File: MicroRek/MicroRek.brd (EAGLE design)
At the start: 40 x 30 mm, 41 parts, among them IC3 LSM9DS1TR

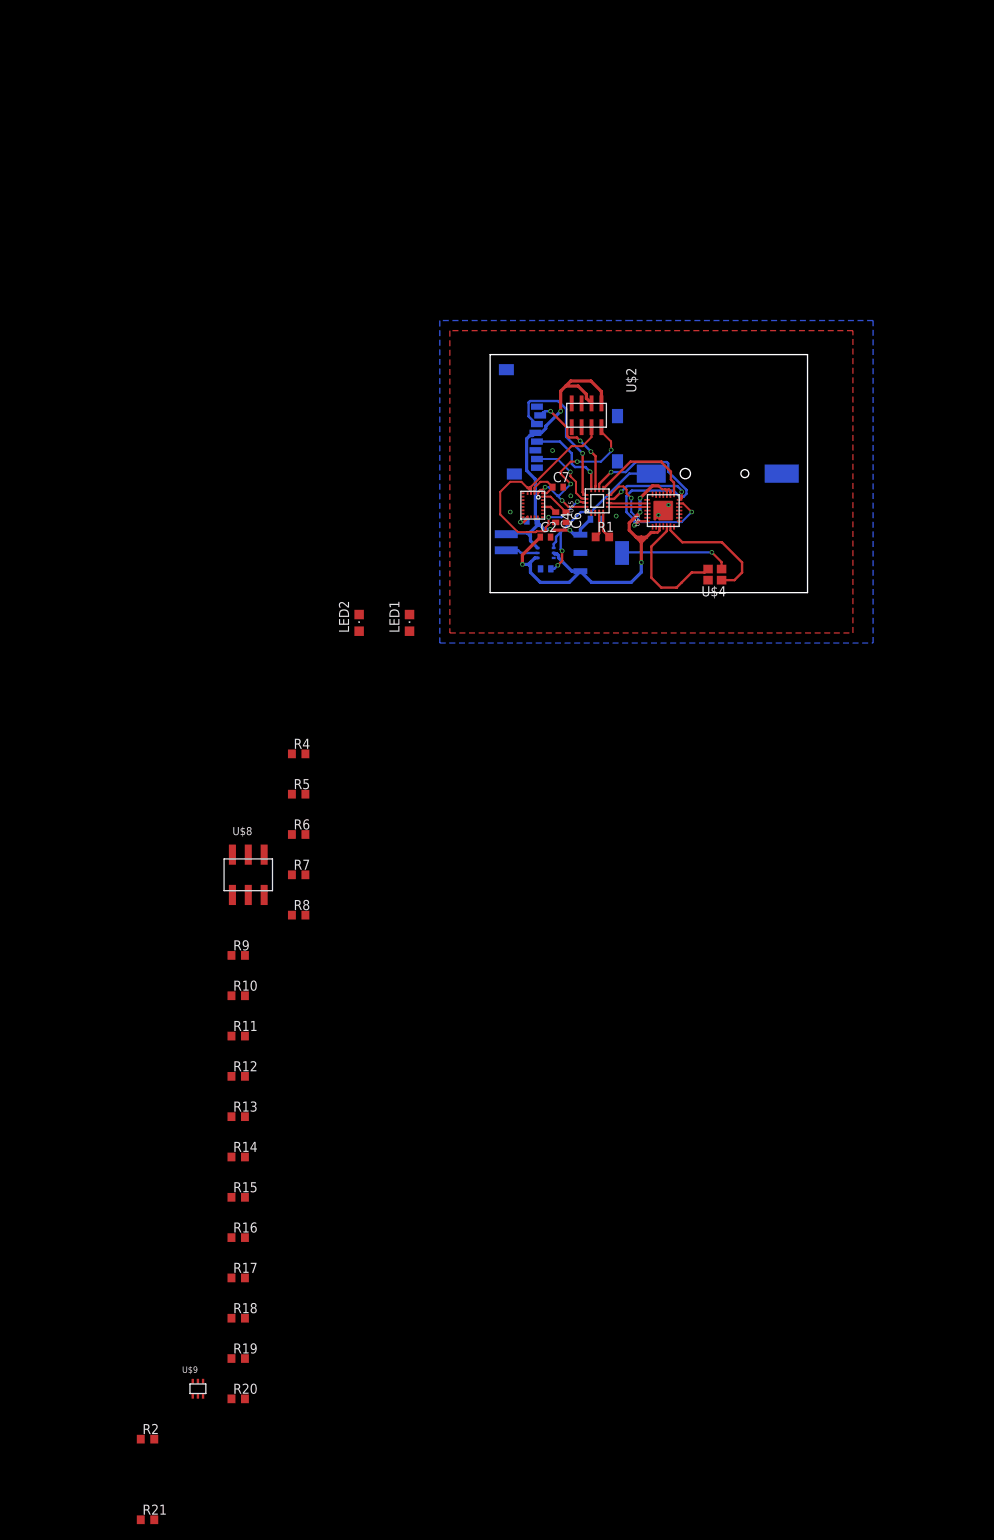
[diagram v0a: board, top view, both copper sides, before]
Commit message: fixed pullup resistors
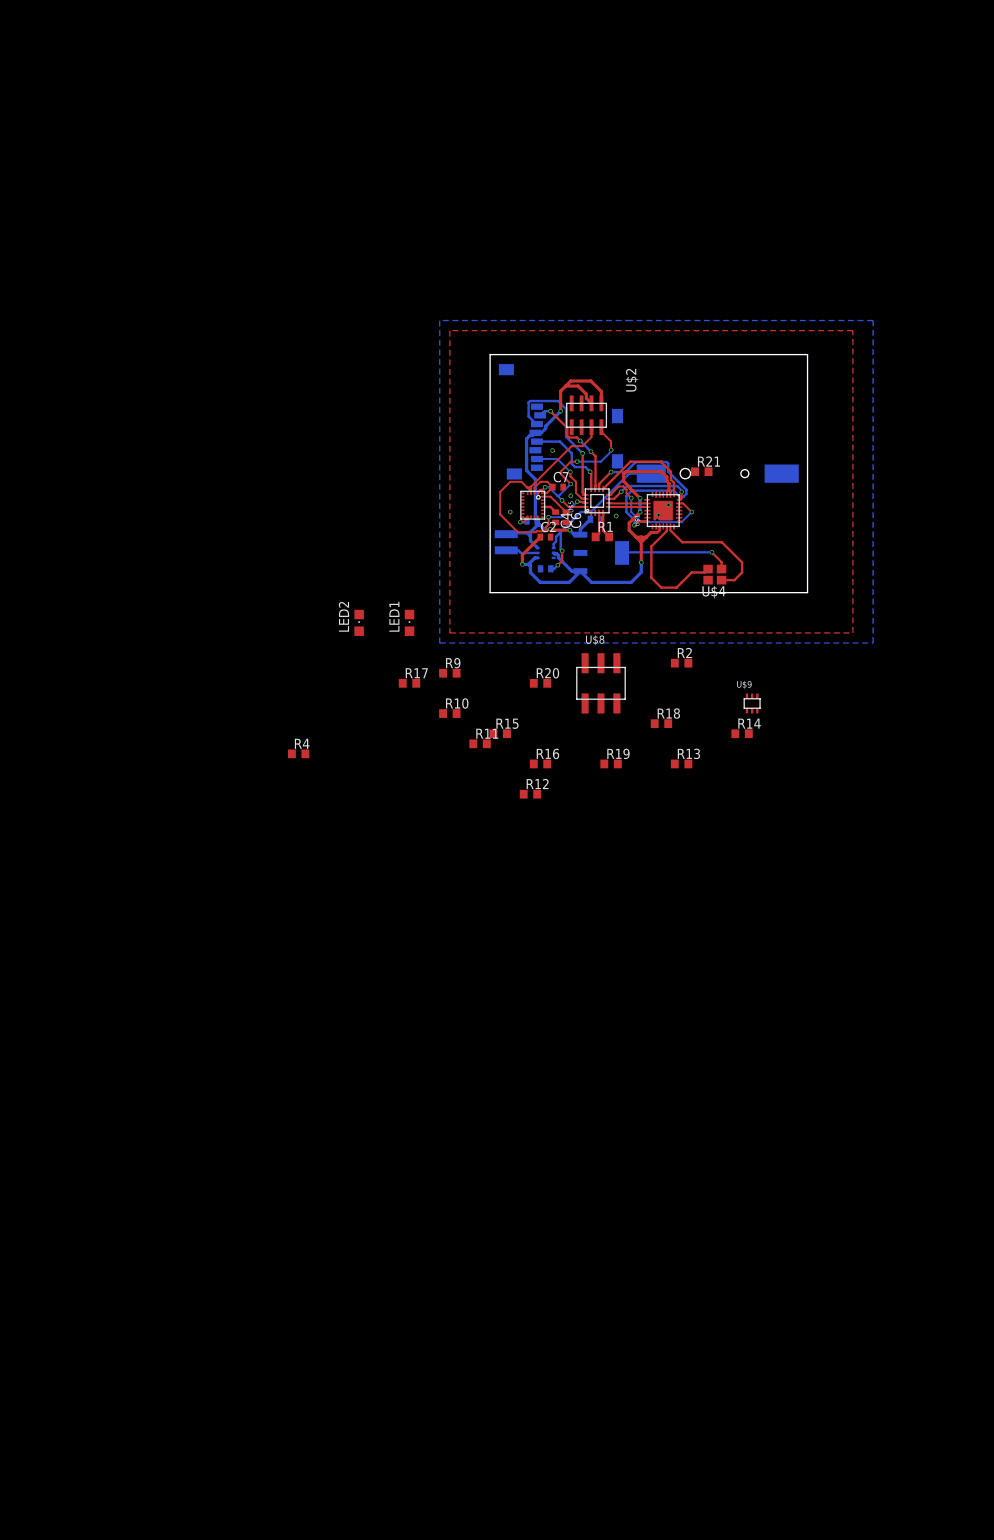
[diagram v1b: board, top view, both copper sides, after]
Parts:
- removed R5, R6, R7, R8: 10kΩ, resistor:R0603
- moved R21 149.4 mm to (26.7, 15.2)
- moved R2 118.7 mm to (24.1, -8.89)
- moved U$9 111.1 mm to (33.0, -14.0)
- moved R20 97.9 mm to (6.35, -11.4)
- moved R18 92.0 mm to (21.6, -16.5)
- moved R19 88.4 mm to (15.2, -21.6)
- moved R14 82.9 mm to (31.8, -17.8)
- moved R17 78.0 mm to (-10.2, -11.4)
- moved R13 71.4 mm to (24.1, -21.6)
- moved R16 70.8 mm to (6.35, -21.6)
- moved R15 67.1 mm to (1.27, -17.8)
- moved R12 51.2 mm to (5.08, -25.4)
- moved U$8 50.6 mm to (14.0, -11.4)
- moved R11 47.8 mm to (-1.27, -19.1)
- moved R9 44.5 mm to (-5.08, -10.2)
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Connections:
- net 3.3V: no longer R7.1, R8.1
- net 5V: no longer R5.2, R6.2
- net SCL3: no longer R8.2
- net SCL5: no longer R6.1
- net SDA3: no longer R7.2
- net SDA5: no longer R5.1
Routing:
- net 5V: track 51.3 -> 58.3 mm

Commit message: started new board layout
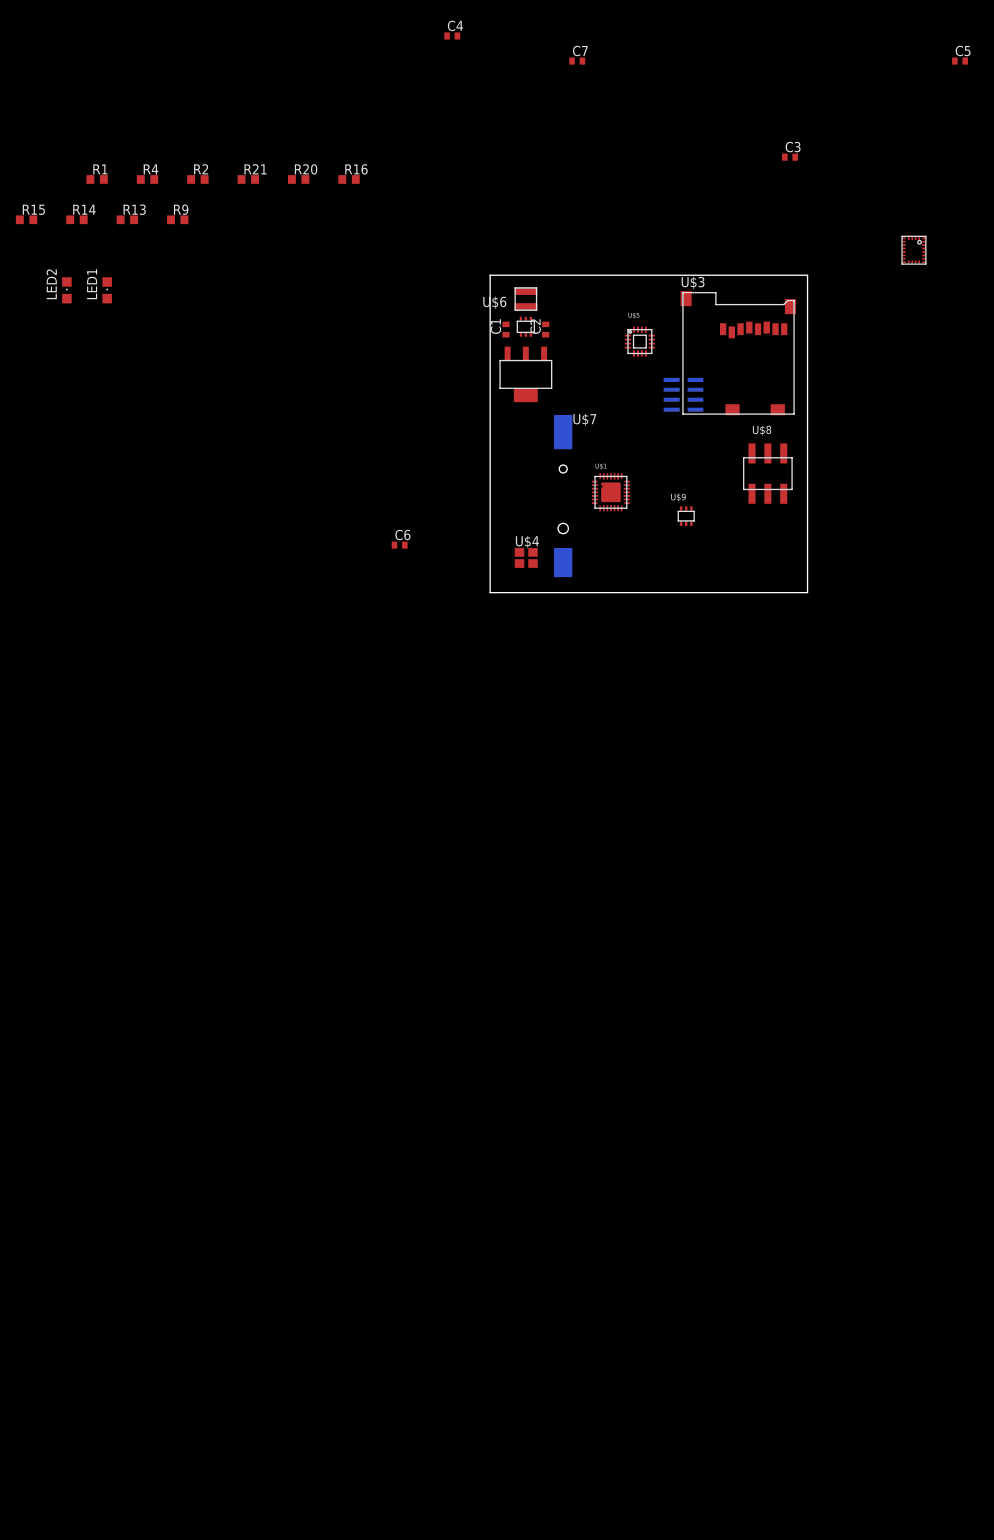
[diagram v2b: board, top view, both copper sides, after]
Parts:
- removed R10, R11, R12, R17, R18, R19: 4.7kΩ, resistor:R0603
- R4: value 100KΩ -> 100Ω
- moved R14 105.9 mm to (-52.1, 47.0)
- moved R13 97.9 mm to (-45.7, 47.0)
- moved R15 88.1 mm to (-58.4, 47.0)
- moved R2 86.2 mm to (-36.8, 52.1)
- moved R1 78.0 mm to (-49.5, 52.1)
- moved R16 77.5 mm to (-17.8, 52.1)
- moved R4 74.9 mm to (-43.2, 52.1)
- moved C5 73.8 mm to (59.2, 67.0), flipped to the top, turned to 0 degrees
- moved R20 70.4 mm to (-24.1, 52.1)
- moved R21 68.0 mm to (-30.5, 52.1)
- moved R9 66.6 mm to (-39.4, 47.0)
- moved C4 62.0 mm to (-4.78, 70.2), turned to 0 degrees
- moved IC3 57.8 mm to (53.4, 43.1)
- moved LED1 56.6 mm to (-48.3, 38.1)
- moved C3 56.2 mm to (37.8, 54.9), flipped to the top
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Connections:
- net 3.3V: no longer R17.1, R18.1, R19.1
- net 5V: no longer R10.2, R11.2, R12.2
- net MISO3: no longer R19.2
- net MISO5: no longer R12.1
- net MOSI3: no longer R18.2
- net MOSI5: no longer R11.1
- net SCK3: no longer R17.2
- net SCK5: no longer R10.1
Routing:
- net 5V: track 58.3 -> 0.00 mm, vias 4 -> 0
- net 3.3V: track 53.8 -> 0.00 mm, vias 3 -> 0
- net SDA3: track 34.9 -> 0.00 mm, vias 2 -> 0
- net D25: track 29.5 -> 0.00 mm, vias 2 -> 0
- net SCL3: track 22.9 -> 0.00 mm, vias 5 -> 0
- net N$2: track 22.4 -> 0.00 mm, vias 2 -> 0
- net MOSI3: track 20.3 -> 0.00 mm, vias 1 -> 0
- net MOSI5: track 16.6 -> 0.00 mm, vias 2 -> 0
- net GND: track 16.1 -> 0.00 mm, vias 8 -> 0
- net CPB6: track 15.9 -> 0.00 mm
- net CPB7: track 15.5 -> 0.00 mm
- net D23: track 14.3 -> 0.00 mm, vias 3 -> 0
- net SCK5: track 13.6 -> 0.00 mm
- net MISO5: track 11.4 -> 0.00 mm, vias 2 -> 0
- net SCK3: track 11.3 -> 0.00 mm, vias 1 -> 0
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- removed copper zone on layer 1, net GND
- removed copper zone on layer 16, net GND
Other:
- board size 40 x 30 mm -> 40 x 40 mm
